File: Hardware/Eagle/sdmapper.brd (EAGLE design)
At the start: 101 x 64.6 mm, 27 parts, among them IC1 AM29F010J, IC2 HM628512ASOP32, IC3 XC95144XL_TQ100, IC4 LM1117-3V3, T1 BC558, T2 BC558

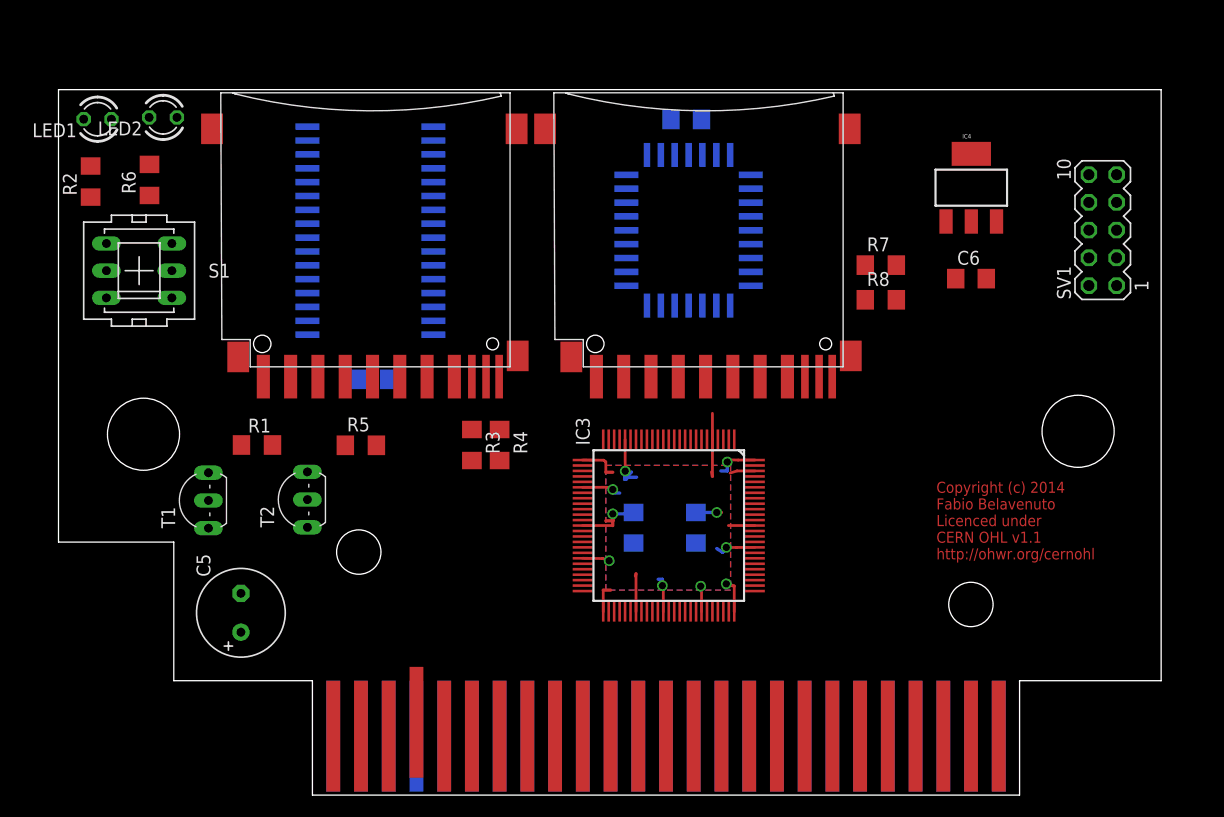
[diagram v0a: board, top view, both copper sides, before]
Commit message: Terminado layout da placa Atualizado esquema.pdf Atualizado pinout no projeto do ISE
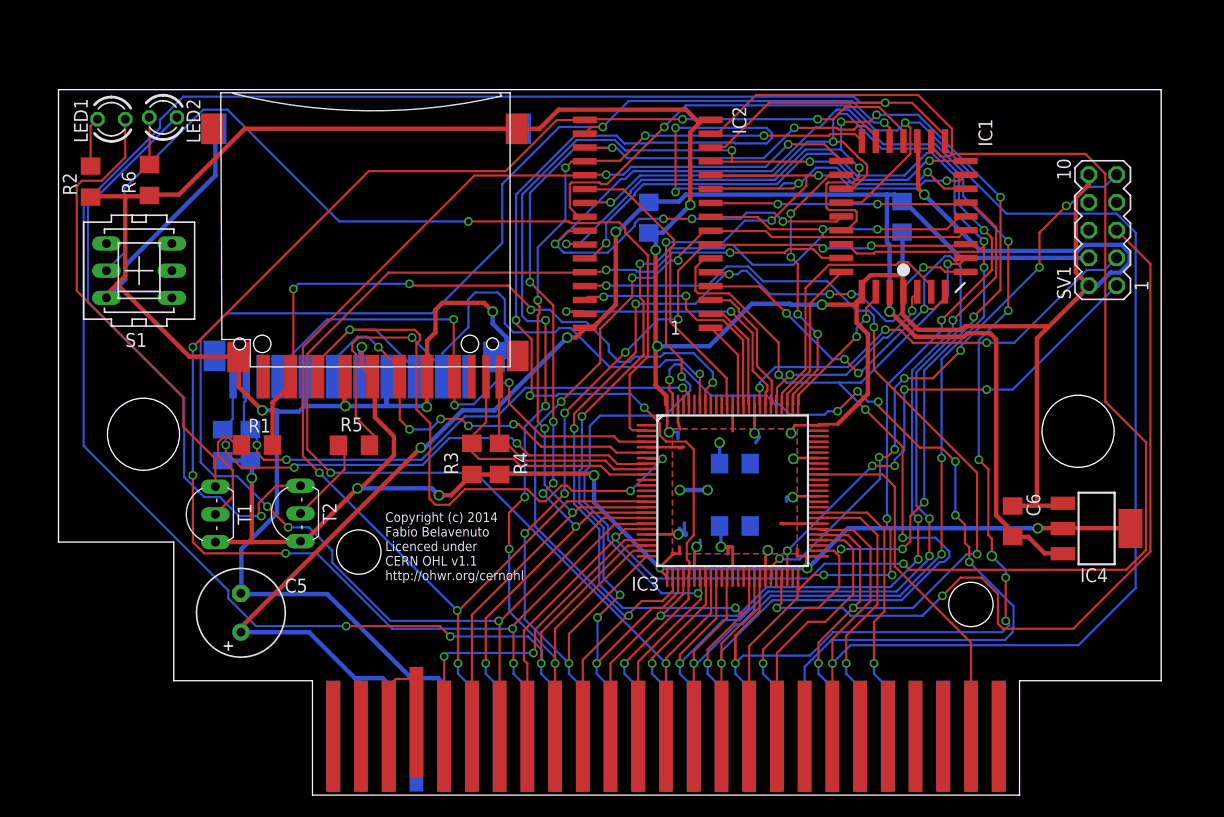
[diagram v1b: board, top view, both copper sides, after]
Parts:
- moved R8 61.7 mm to (15.3, 31.7), flipped to the bottom, turned to 270 degrees
- moved R7 60.1 mm to (17.8, 31.7), flipped to the bottom, turned to 270 degrees
- moved IC4 33.3 mm to (95.3, 24.1), turned to 270 degrees
- moved U$2 30.5 mm to (28.4, 38.9), flipped to the bottom
- moved C4 29.2 mm to (54.3, 52.6), turned to 90 degrees
- moved IC2 25.4 mm to (54.2, 52.0), flipped to the top
- moved C6 22.5 mm to (87.6, 24.8), turned to 270 degrees
- moved C3 21.7 mm to (77.5, 52.7), turned to 90 degrees
- moved IC1 19.7 mm to (77.6, 52.7), flipped to the top
- moved C2 9.28 mm to (62.2, 24.3), turned to 0 degrees
- moved C1 6.87 mm to (62.2, 30.0), turned to 0 degrees
- moved IC3 6.66 mm to (62.0, 27.6), turned to 0 degrees
- moved T1 1.42 mm to (13.3, 25.4)
- moved T2 1.42 mm to (21.1, 25.5)
- moved LED1 1.27 mm to (5.08, 61.6)
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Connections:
- net CPU_A0: now also IC3.32; no longer IC3.61
- net CPU_A1: now also IC3.30; no longer IC3.60
- net CPU_A10: now also IC3.50; no longer IC3.76
- net CPU_A11: now also IC3.43; no longer IC3.68
- net CPU_A12: now also IC3.35; no longer IC3.64
- net CPU_A13: now also IC3.34; no longer IC3.63
- net CPU_A14: now also IC3.33; no longer IC3.40
- net CPU_A15: now also IC3.54; no longer IC3.71
- net CPU_A2: now also IC3.29; no longer IC3.59
- net CPU_A3: now also IC3.28; no longer IC3.58
- net CPU_A4: now also IC3.27; no longer IC3.43
- net CPU_A5: now also IC3.25; no longer IC3.56
- net CPU_A6: now also IC3.42; no longer IC3.67
- net CPU_A7: now also IC3.41; no longer IC3.66
- net CPU_A8: now also IC3.37; no longer IC3.65
- net CPU_A9: now also IC3.52; no longer IC3.70
- net CPU_D0: now also IC3.24; no longer IC3.55
- net CPU_D1: now also IC3.23; no longer IC3.54
- net CPU_D2: now also IC3.20; no longer IC3.42
- net CPU_D3: now also IC3.19; no longer IC3.46
- net CPU_D4: now also IC3.18; no longer IC3.53
- net CPU_D5: now also IC3.17; no longer IC3.52
- net CPU_D6: now also IC3.16; no longer IC3.49
- net CPU_D7: now also IC3.15; no longer IC3.50
- net CPU_IORQ: now also IC3.58; no longer IC3.73
- net CPU_M1: now also IC3.59; no longer IC3.77
- net CPU_RD: now also IC3.56; no longer IC3.72
- net CPU_WR: now also IC3.55; no longer IC3.74
- net DIS_MAPPER: now also IC3.2; no longer IC3.79
- net GND: now also IC1.1, IC1.30
- net RAM_A14: now also IC3.81; no longer IC3.36
- net RAM_A16: now also IC3.85; no longer IC3.39
- net RAM_A17: now also IC3.86; no longer IC3.90
- net RAM_A18: now also IC3.87; no longer IC3.41
- net RAM_CS: now also IC3.89; no longer IC3.92
- net ROM_A14: now also IC3.78; no longer IC3.94
- net ROM_A15: now also IC3.79; no longer IC3.96
- net ROM_A16: now also IC3.80; no longer IC3.95
- net ROM_CS: now also IC3.77; no longer IC3.91
- net ROM_WE: now also IC3.76; no longer IC3.97
- net SD_CD0: now also IC3.10; no longer IC3.34
- net SD_CD1: now also IC3.96; no longer IC3.25
- net SD_CS0: now also IC3.93; no longer IC3.29
- net SD_CS1: now also IC3.94; no longer IC3.28
- net SD_MISO: now also IC3.4; no longer IC3.35
- net SD_MOSI: now also IC3.7; no longer IC3.32
- net SD_SCLK: now also IC3.6; no longer IC3.33
- net SD_WP0: now also IC3.9; no longer IC3.37
- net SD_WP1: now also IC3.8; no longer IC3.30
- net SLTSL: now also IC3.66; no longer IC3.78
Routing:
- net GND: track 30.7 -> 407.7 mm, vias 8 -> 18
- net CPU_D1: track 0.00 -> 199.6 mm, vias 0 -> 4
- net VCC: track 0.00 -> 174.3 mm, vias 0 -> 4
- net CPU_A11: track 0.00 -> 164.9 mm, vias 0 -> 11
- net CPU_RD: track 0.00 -> 163.1 mm, vias 0 -> 3
- net CPU_D2: track 0.00 -> 157.7 mm, vias 0 -> 2
- net CPU_D3: track 0.00 -> 153.2 mm, vias 0 -> 7
- net CPU_D4: track 0.00 -> 152.7 mm, vias 0 -> 5
- net CPU_A1: track 0.00 -> 145.6 mm, vias 0 -> 8
- net CPU_A8: track 0.00 -> 135.4 mm, vias 0 -> 6
- net CPU_A9: track 0.00 -> 130.1 mm, vias 0 -> 10
- net +3V3: track 30.5 -> 155.5 mm, vias 2 -> 12
- net CPU_D7: track 0.00 -> 121.1 mm, vias 0 -> 5
- net CPU_A13: track 0.00 -> 119.4 mm, vias 0 -> 4
- net CPU_D0: track 0.00 -> 116.7 mm, vias 0 -> 8
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
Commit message: Corrigido footprint da SRAM Retirado LEDs comuns e trocado por LED bi-color Layout da placa foi otimizada
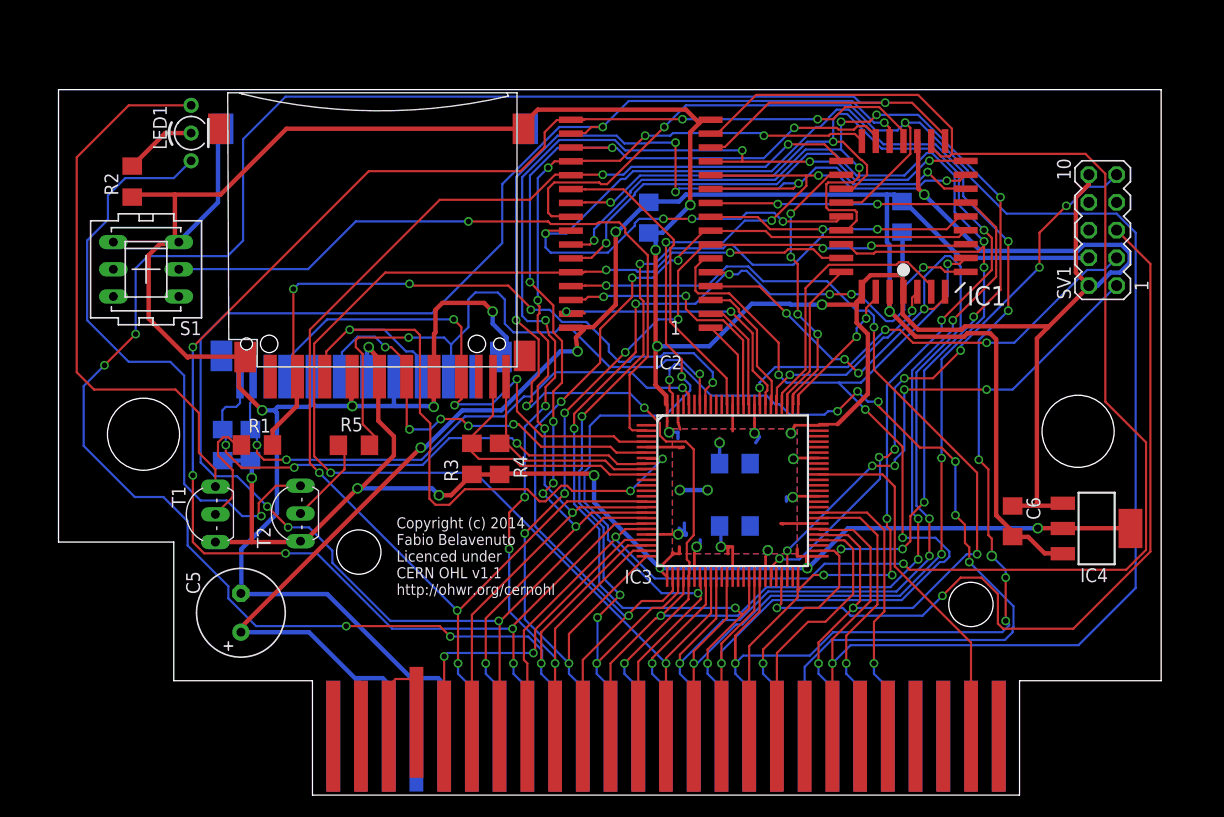
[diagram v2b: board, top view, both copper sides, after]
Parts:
- removed LED2: SD2, led:LED3MM
- removed R6: 330, rcl:R1206
- LED1: value SD1 -> (none); device led:LED3MM -> led_duoled:DUOLED-C-3MM
- moved LED1 7.41 mm to (12.4, 60.3), turned to 270 degrees
- moved R2 3.81 mm to (6.99, 55.9)
- moved S1 0.65 mm to (8.26, 47.8), turned to 180 degrees
- moved U$1 0.63 mm to (29.0, 38.9)
- moved U$2 0.63 mm to (29.1, 38.9)
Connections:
- removed net N$7: LED2.K, R6.2
- net GND: no longer R6.1
- net N$2: now also LED1.1; no longer LED1.A
- net N$3: now also LED1.2; no longer LED1.K
- net N$8: now also LED1.3; no longer LED2.A
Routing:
- net DIS_MAPPER: track 83.1 -> 64.5 mm
- net CPU_A1: track 145.6 -> 129.2 mm
- net GND: track 407.7 -> 393.7 mm
- net N$2: track 41.8 -> 52.2 mm
- net N$7: track 4.33 -> 0.00 mm
- net VCC: track 174.3 -> 177.5 mm
- net CPU_D3: track 153.2 -> 156.3 mm
- net CPU_D5: track 101.8 -> 104.6 mm
- net CPU_RD: track 163.1 -> 165.8 mm
- net CPU_D0: track 116.7 -> 119.2 mm
- net N$3: track 4.56 -> 6.65 mm
- net CPU_A13: track 119.4 -> 121.3 mm
- net CPU_D6: track 94.1 -> 96.1 mm
- net N$8: track 54.3 -> 56.1 mm
- net CPU_A11: track 164.9 -> 166.6 mm
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
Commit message: Otimização na placa utilitário de gravação reconhece mais marcas/modelos de flash adicionado binários do driver e atualizador
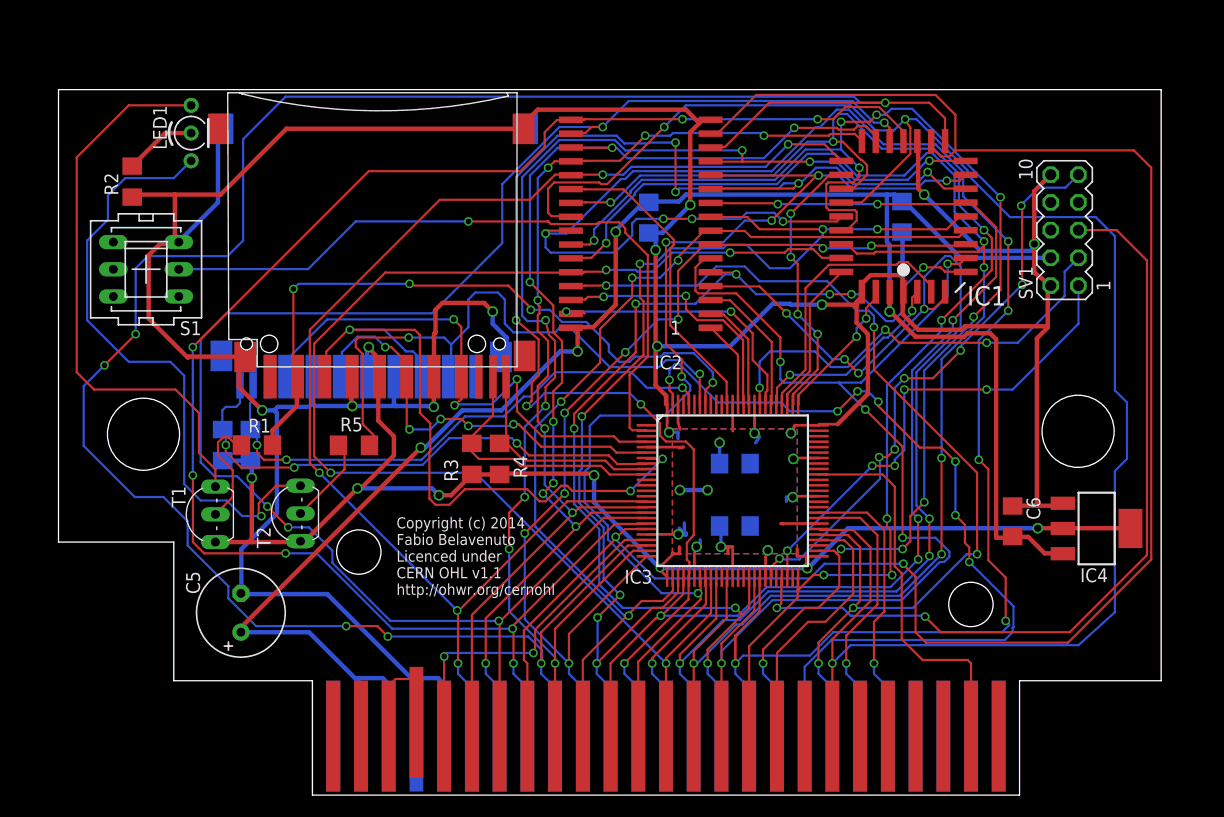
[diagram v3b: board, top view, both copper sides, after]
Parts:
- moved SV1 3.49 mm to (92.4, 51.4)
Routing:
- net GND: track 393.7 -> 378.5 mm, vias 18 -> 19
- net CPU_D2: track 157.7 -> 171.2 mm
- net VCC: track 177.5 -> 174.5 mm
- net SLTSL: track 33.2 -> 35.6 mm
- net TCK: track 46.2 -> 44.8 mm
- net CPU_RD: track 165.8 -> 164.5 mm
- net TMS: track 76.1 -> 75.1 mm
- net TDI: track 54.2 -> 53.2 mm
- net CPU_D1: track 199.9 -> 200.8 mm
- net CPU_A6: track 103.6 -> 104.1 mm
- net CPU_A11: track 166.6 -> 167.1 mm, vias 11 -> 9

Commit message: Modificado porta SPI no CPLD para trabalhar assincronicamente. Adicionado oscilador de 25MHz na placa. Modificado porta de controle do updater. Estudando desenvolvimento do driver para Symbos
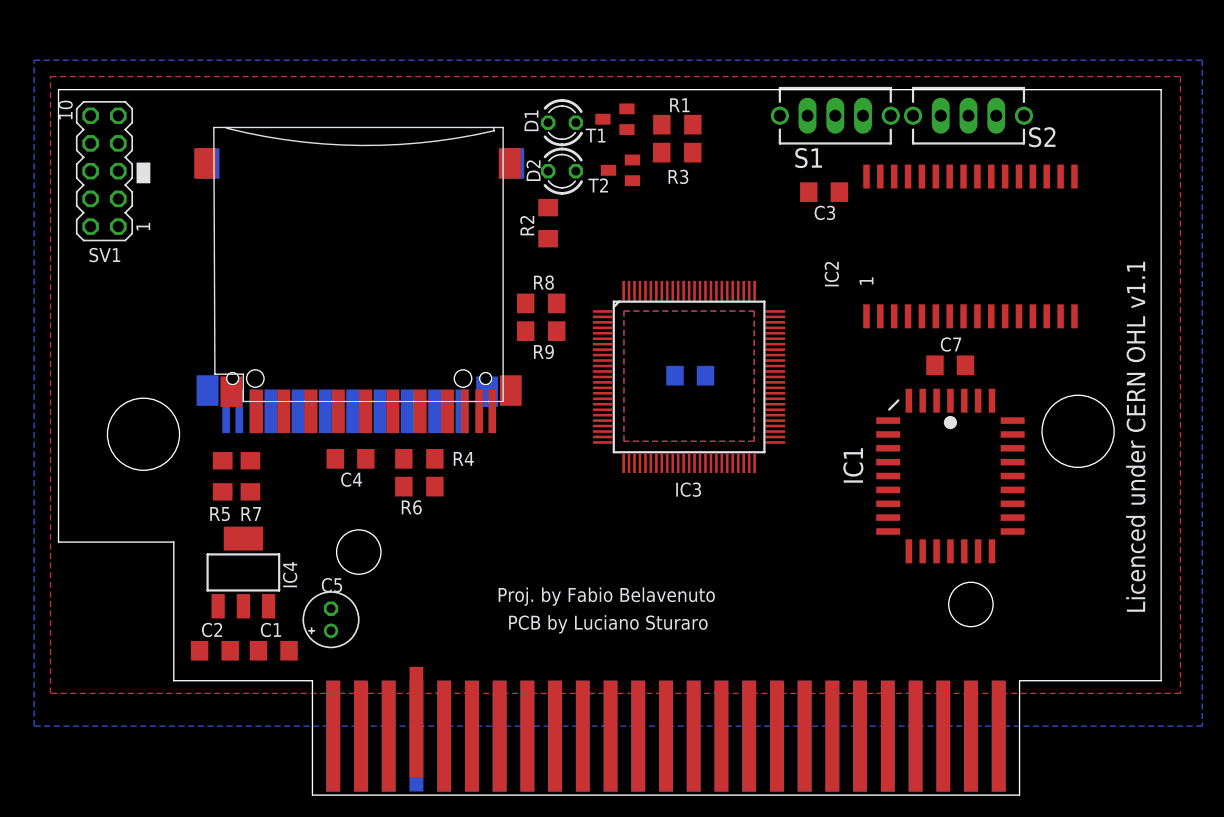
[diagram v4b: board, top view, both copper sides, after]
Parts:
- removed LED1: (no value), led_duoled:DUOLED-C-3MM
- removed U$1, U$2: SDMMC06132, adafruit:06132
- added C7: 100n, rcl:C1206
- added D1: Cart1, led:LED3MM
- added D2: Cart2, led:LED3MM
- added R6, R9: 4K7, rcl:R1206
- added S2: TL32YO, switch:TL3XYO
- added SD1, SD2: SDMMC06132, adafruit:06132
- C5: device rcl:E3,5-8 -> rcl:E2-5
- S1: value PVA2R -> TL32YO; device switch-misc:PVA2R -> switch:TL3XYO
- T1, T2: value BC558 -> BC857; device transistor:TO92-EBC -> transistor:SOT23-BEC
- moved SV1 88.1 mm to (4.45, 56.8)
- moved IC4 78.3 mm to (17.2, 20.1), turned to 0 degrees
- moved S1 64.7 mm to (71.4, 61.9), turned to 0 degrees
- moved T1 52.4 mm to (51.2, 61.6)
- moved C2 49.0 mm to (14.6, 12.9), flipped to the top
- moved R1 48.4 mm to (56.9, 61.1)
- moved C1 45.6 mm to (20.0, 12.9), flipped to the top
- moved T2 43.8 mm to (51.7, 56.9)
- moved R2 38.3 mm to (45.1, 52.1)
- moved C4 35.1 mm to (27.0, 30.5), flipped to the top, turned to 0 degrees
- moved R3 33.8 mm to (56.9, 58.5), turned to 0 degrees
- moved C6 32.4 mm to (58.1, 38.1), flipped to the bottom, turned to 0 degrees
- moved R8 31.9 mm to (44.5, 44.7), flipped to the top, turned to 180 degrees
- moved IC2 29.7 mm to (83.8, 49.3), turned to 0 degrees
- moved IC1 24.2 mm to (81.9, 28.9), turned to 0 degrees
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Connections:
- removed net DIS_MAPPER: IC3.2, S1.2
- removed net N$2: LED1.1, T1.C
- removed net N$3: LED1.2, R2.2
- new net DIS_MR_MP: IC3.2, R9.1, S1.2
- new net MR_MP: IC3.1, R8.1, S2.2
- new net N$7: D1.K, D2.K, R2.2
- new net N$9: D2.A, T2.C
- new net RAM_A13: IC2.28, IC3.70
- new net RAM_WE: IC2.29, IC3.65
- net +3V3: now also C4.2, C6.2, C7.2, R5.2, R6.2, R9.2, SD1.4, SD2.4; no longer C1.2, R3.2, U$1.4, U$2.4
- net CPU_A13: no longer IC2.28
- net CPU_WR: no longer IC2.29
- net GND: now also C7.1, S1.1, S2.1, SD1.3, SD1.6, SD1.GP, SD1.GP3, SD2.3, SD2.6, SD2.GP, SD2.GP3; no longer S1.3, U$1.3, U$1.6, U$1.GP, U$1.GP3, U$2.3, U$2.6, U$2.GP, U$2.GP3
- net N$5: now also R3.1; no longer R5.1
- net N$8: now also D1.A, T1.C; no longer LED1.3, T2.C
- net SD_CD0: now also R4.1, SD1.CD; no longer R3.1, U$1.CD
- net SD_CD1: now also SD2.CD; no longer U$2.CD
- net SD_CS0: now also SD1.1; no longer U$1.1
- net SD_CS1: now also R3.2, SD2.1; no longer R5.2, U$2.1
- net SD_MISO: now also SD1.7, SD2.7; no longer U$1.7, U$2.7
- net SD_MOSI: now also SD1.2, SD2.2; no longer U$1.2, U$2.2
- net SD_SCLK: now also SD1.5, SD2.5; no longer U$1.5, U$2.5
- net SD_WP0: now also R6.1, SD1.WP; no longer R4.1, U$1.WP
- net SD_WP1: now also R5.1, SD2.WP; no longer R8.1, U$2.WP
- net VCC: now also C1.2; no longer C4.2, C6.2
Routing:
- net GND: track 378.5 -> 0.00 mm, vias 19 -> 0
- net CPU_D1: track 200.8 -> 0.00 mm, vias 6 -> 0
- net VCC: track 174.5 -> 0.00 mm, vias 4 -> 0
- net CPU_D2: track 171.2 -> 0.00 mm, vias 2 -> 0
- net CPU_A11: track 167.1 -> 0.00 mm, vias 9 -> 0
- net CPU_RD: track 164.5 -> 0.00 mm, vias 3 -> 0
- net CPU_D3: track 156.3 -> 0.00 mm, vias 7 -> 0
- net +3V3: track 155.1 -> 0.00 mm, vias 12 -> 0
- net CPU_D4: track 153.9 -> 0.00 mm, vias 5 -> 0
- net CPU_A8: track 136.6 -> 0.00 mm, vias 6 -> 0
- net CPU_A1: track 129.2 -> 0.00 mm, vias 8 -> 0
- net CPU_A9: track 129.0 -> 0.00 mm, vias 10 -> 0
- net CPU_A13: track 121.3 -> 0.00 mm, vias 4 -> 0
- net CPU_D7: track 121.2 -> 0.00 mm, vias 5 -> 0
- net CPU_D0: track 119.2 -> 0.00 mm, vias 8 -> 0
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- added copper zone on layer 1, net GND
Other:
- board text added: "Licenced under CERN OHL v1.1"
- board text added: "PCB by Luciano Sturaro"
- board text added: "Proj. by Fabio Belavenuto"
- board text removed: "Copyright (c) 2014 Fabio Belavenuto Licenced under CERN OHL v1.1 http://ohwr.org/cernohl"
